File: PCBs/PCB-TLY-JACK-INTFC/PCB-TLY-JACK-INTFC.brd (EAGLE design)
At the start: 60 x 31 mm, 8 parts

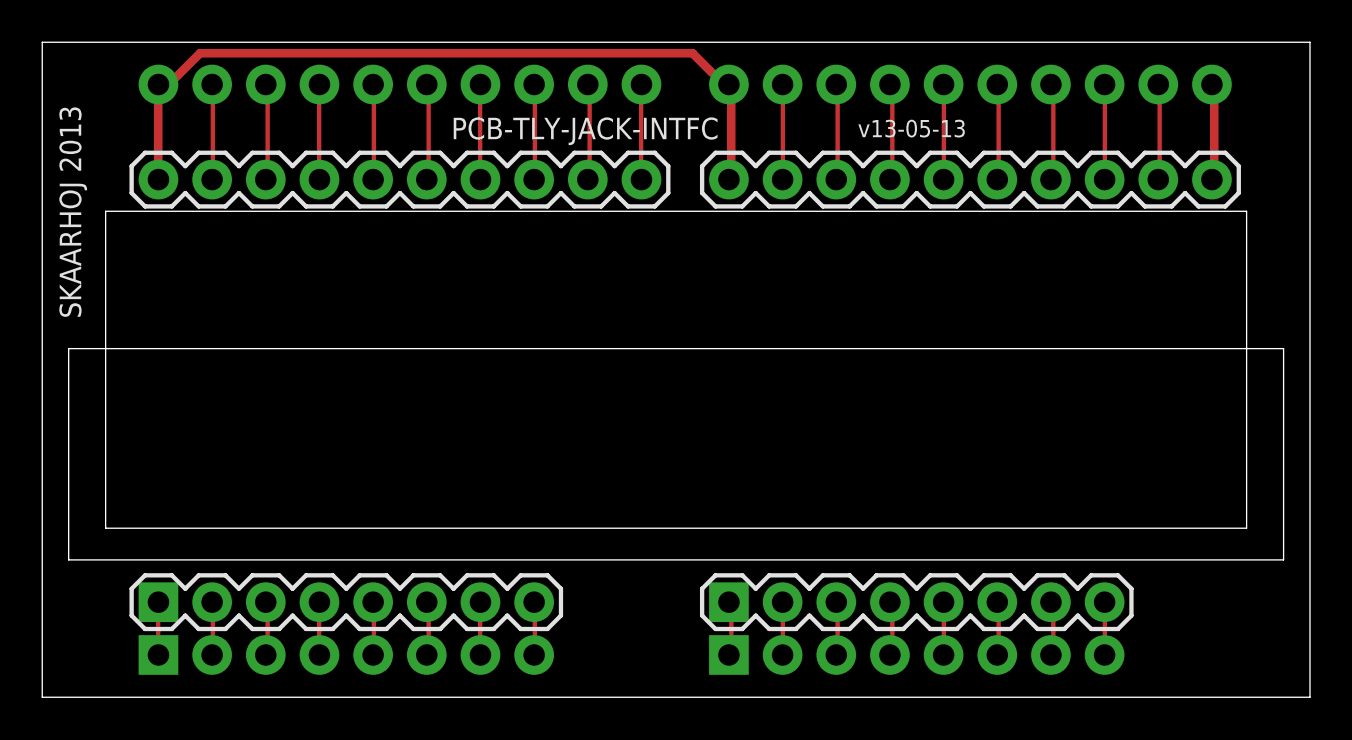
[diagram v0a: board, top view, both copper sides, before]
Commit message: Updated boards
Updated boards with logo before first sending to Alma.
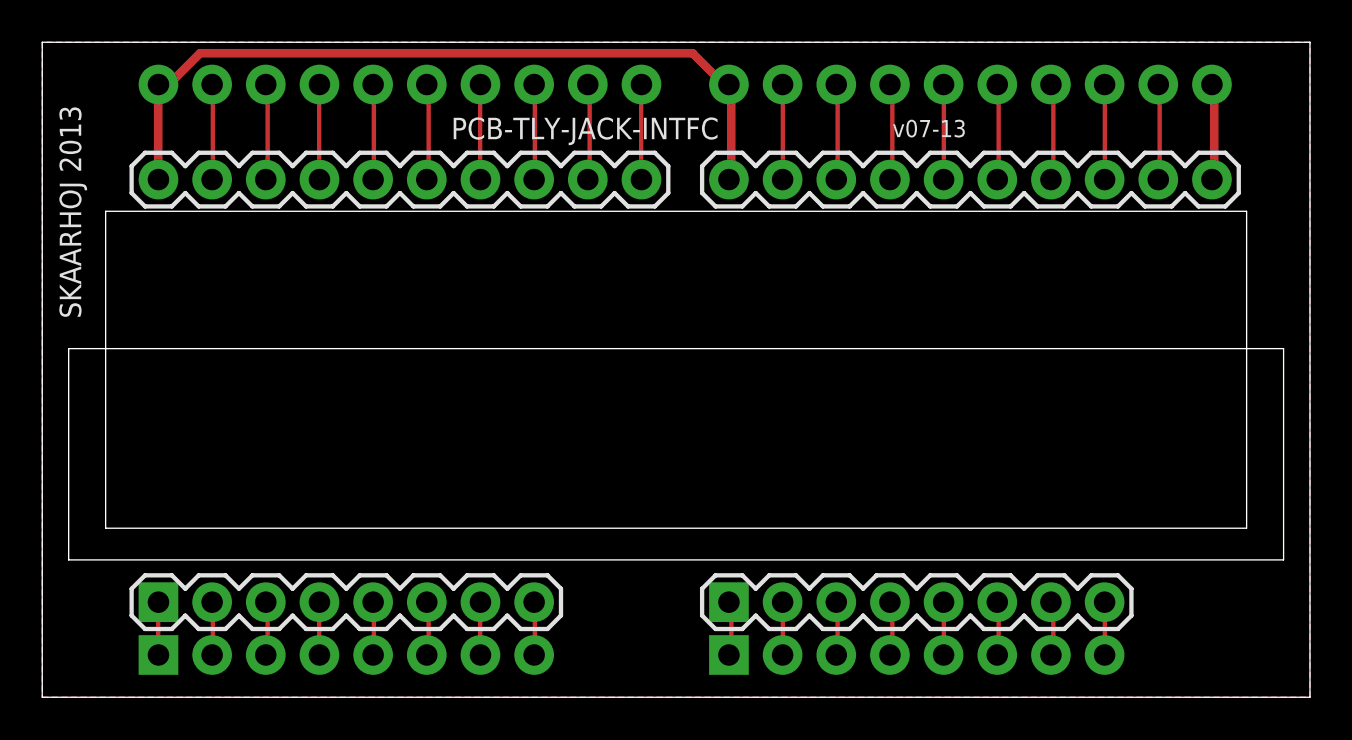
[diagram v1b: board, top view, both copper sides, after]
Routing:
- added copper zone on layer 1, net GND
- added copper zone on layer 16, net GND
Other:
- board text added: "v07-13"
- board text removed: "v13-05-13"
